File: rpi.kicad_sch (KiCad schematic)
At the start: 13 parts, among them J18 Raspberry_Pi_2_3, U16 MCP2518FD-xQBB, U19 SN65HVD230, Y2 40MHz

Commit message: Add title to all schematics pages
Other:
- title: (none) -> RaspberryPi
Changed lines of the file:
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@@
 	(paper "A4")
 	(title_block
+		(title "RaspberryPi")
 		(rev "1")
 	)

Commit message: Redesign board to fit within 102mm x 102mm
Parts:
- U16: now left out of the parts list
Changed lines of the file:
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@@
 		(unit 1)
 		(exclude_from_sim no)
-		(in_bom yes)
+		(in_bom no)
 		(on_board yes)
 		(dnp no)

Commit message: Decrease size of raspberry pi mounting holes
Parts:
- H1, H2, H3, H4: footprint MountingHole:MountingHole_3.2mm_M3_DIN965 -> MountingHole:MountingHole_2.7mm_M2.5_DIN965
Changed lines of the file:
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@@
 			)
 		)
-		(property "Footprint" "MountingHole:MountingHole_3.2mm_M3_DIN965"
+		(property "Footprint" "MountingHole:MountingHole_2.7mm_M2.5_DIN965"
 			(at 20.32 176.53 0)
 			(effects
@@
 			)
 		)
-		(property "Footprint" "MountingHole:MountingHole_3.2mm_M3_DIN965"
+		(property "Footprint" "MountingHole:MountingHole_2.7mm_M2.5_DIN965"
 			(at 20.32 181.61 0)
 			(effects
@@
 			)
 		)
-		(property "Footprint" "MountingHole:MountingHole_3.2mm_M3_DIN965"
+		(property "Footprint" "MountingHole:MountingHole_2.7mm_M2.5_DIN965"
 			(at 20.32 191.77 0)
 			(effects
@@
 			)
 		)
-		(property "Footprint" "MountingHole:MountingHole_3.2mm_M3_DIN965"
+		(property "Footprint" "MountingHole:MountingHole_2.7mm_M2.5_DIN965"
 			(at 20.32 186.69 0)
 			(effects

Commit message: Update production data
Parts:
- U19: JLCPCB Rotation Offset -90 -> 0
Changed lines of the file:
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@@
 			)
 		)
-		(property "JLCPCB Rotation Offset" "-90"
+		(property "JLCPCB Rotation Offset" "0"
 			(at 257.81 134.62 0)
 			(effects

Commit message: Replace RPi connector
New variant is SMD type and has been rotated.
Closes #16 and #11
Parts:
- removed H1, H2, H3, H4: MountingHole, MountingHole:MountingHole_2.7mm_M2.5_DIN965, symbol Mechanical:MountingHole
- J18: footprint Connector_PinSocket_2.54mm:PinSocket_2x20_P2.54mm_Vertical -> Connector_PinSocket_2.54mm:PinSocket_2x20_P2.54mm_Vertical_SMD; LCSC C110426 -> C2685092; now in the parts list

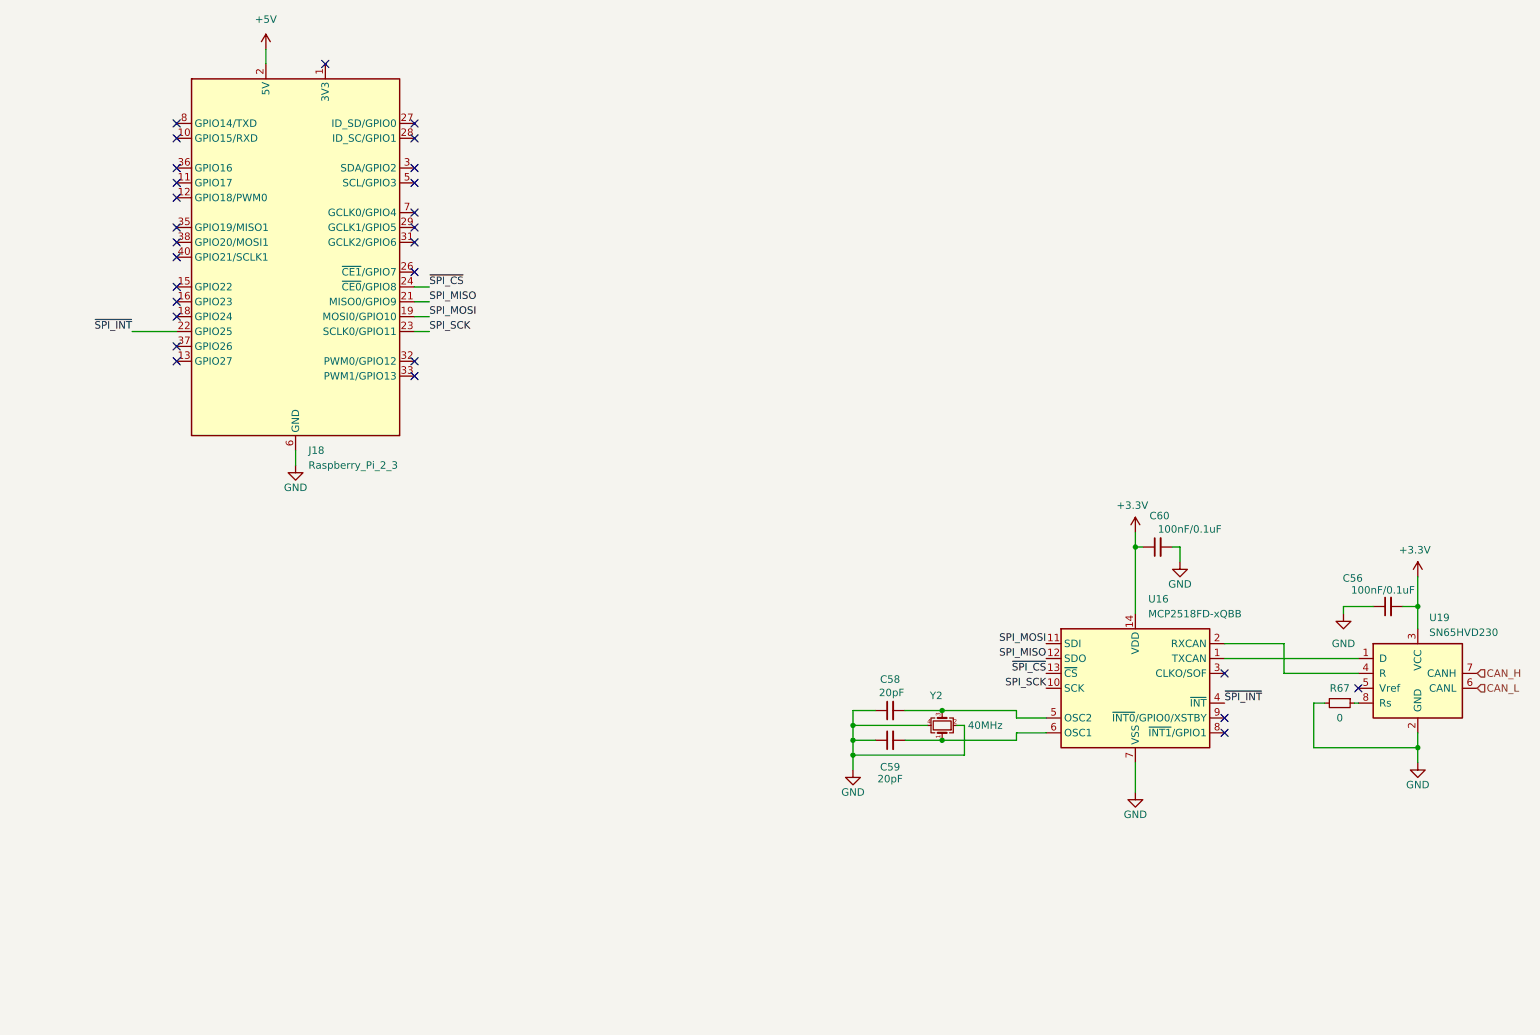
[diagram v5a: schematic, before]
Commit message: Add RPi ID EEPROM
Closes #15
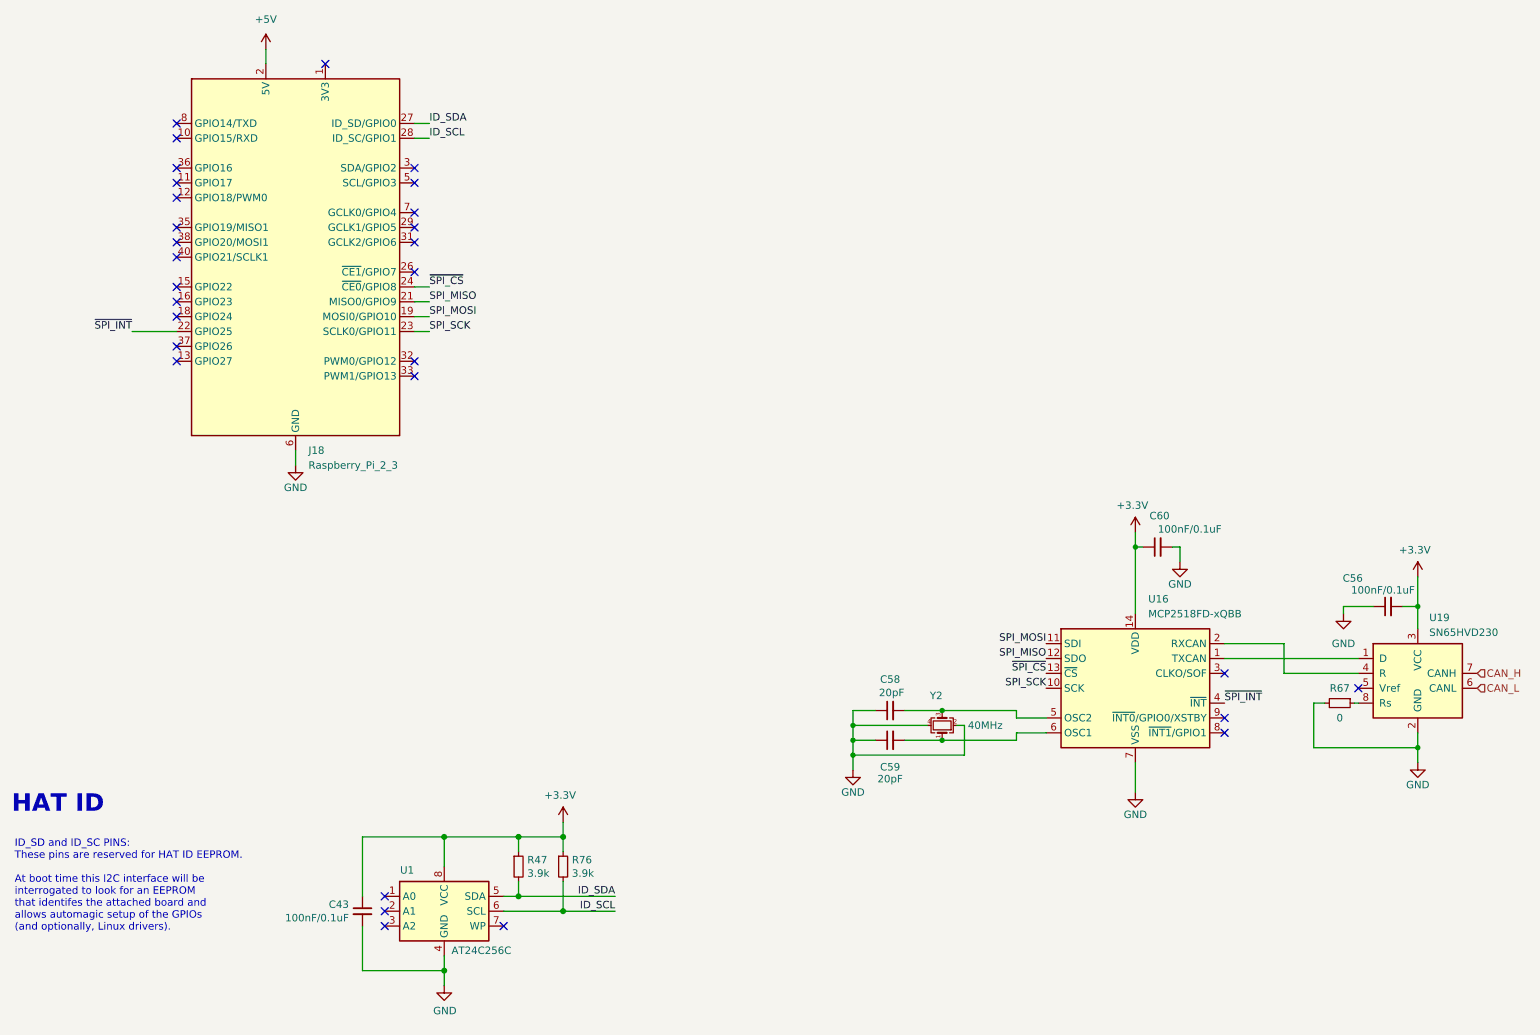
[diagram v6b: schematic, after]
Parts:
- added C43: 100nF/0.1uF, Capacitor_SMD:C_0603_1608Metric, symbol Device:C_Small
- added R47, R76: 3.9k, Resistor_SMD:R_0603_1608Metric, symbol Device:R_Small
- added U1: AT24C256C, Package_SO:SOIC-8_3.9x4.9mm_P1.27mm, symbol Memory_EEPROM:CAT24C256
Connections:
- net +3.3V: now also C43.1, R47.1, R76.1, U1.8 (VCC)
- net GND: now also C43.2, U1.4 (GND)
- net ID_SDA: now reaches J18.27 (ID_SD/GPIO0)
- net ID_SDA: now also R47.2, U1.5 (SDA)
- net ID_SCL: now reaches J18.28 (ID_SC/GPIO1)
- net ID_SCL: now also R76.2, U1.6 (SCL)
- no-connect marks 28 -> 30
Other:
- note added: "HAT ID"
- note added: "ID_SD and ID_SC PINS: These pins are reserved for HAT ID EEPROM. At boot time this I2C interface will be interrogated to look for an EEPROM that identifes the attached board and allows automagic setup of the GPIOs (and optionally, Linux drivers)."

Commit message: Fix manufaturing properties
Such as rotations
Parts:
- J18: JLCPCB Rotation Offset (none) -> 90
- U16: now in the parts list
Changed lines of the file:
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@@
 			)
 		)
-		(property "LCSC alt" ""
+		(property "JLCPCB Rotation Offset" "90"
 			(at 66.04 63.5 0)
 			(effects
@@
 		(unit 1)
 		(exclude_from_sim no)
-		(in_bom no)
-		(on_board yes)
-		(dnp no)
+		(in_bom yes)
+		(on_board yes)
+		(dnp no)
